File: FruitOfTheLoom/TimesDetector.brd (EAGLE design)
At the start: 73 x 68.9 mm, 22 parts

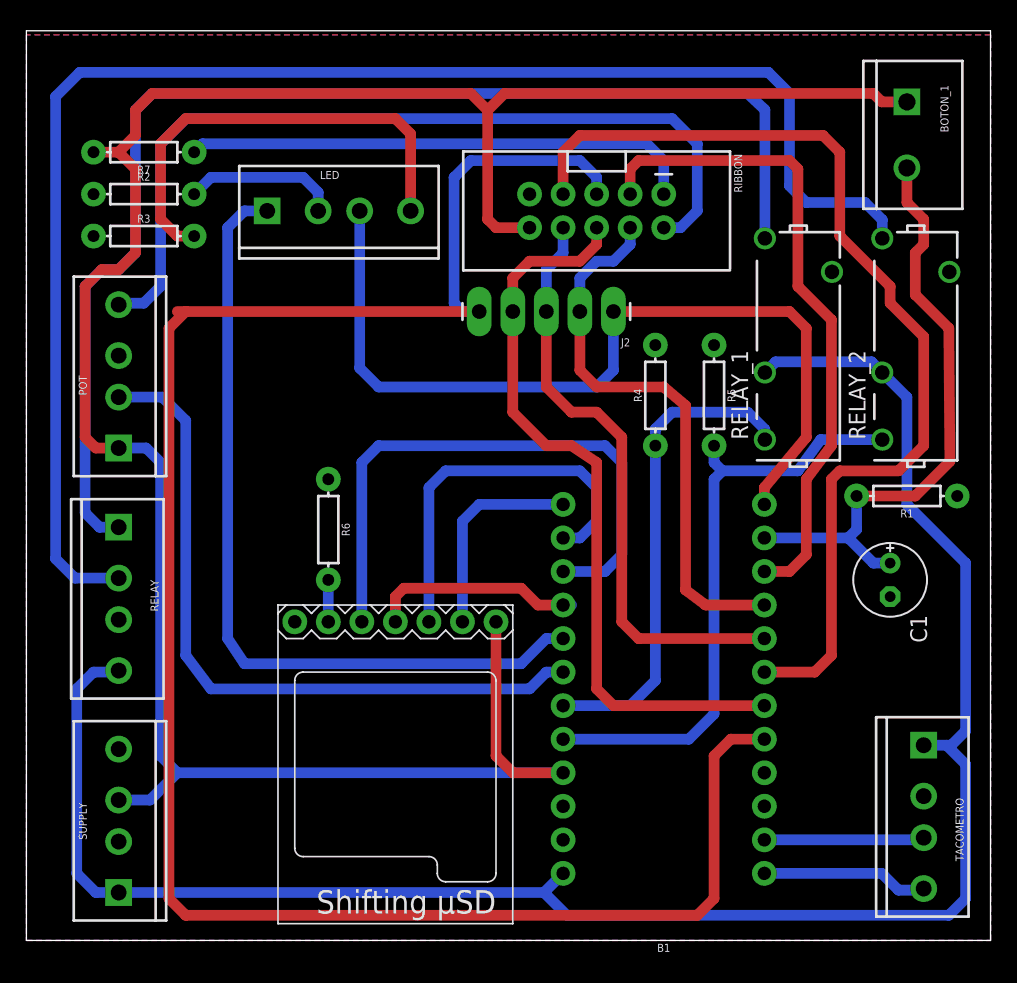
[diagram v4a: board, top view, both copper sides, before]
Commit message: Correcion de pistas, generacion de pdf listos para revelar PCB
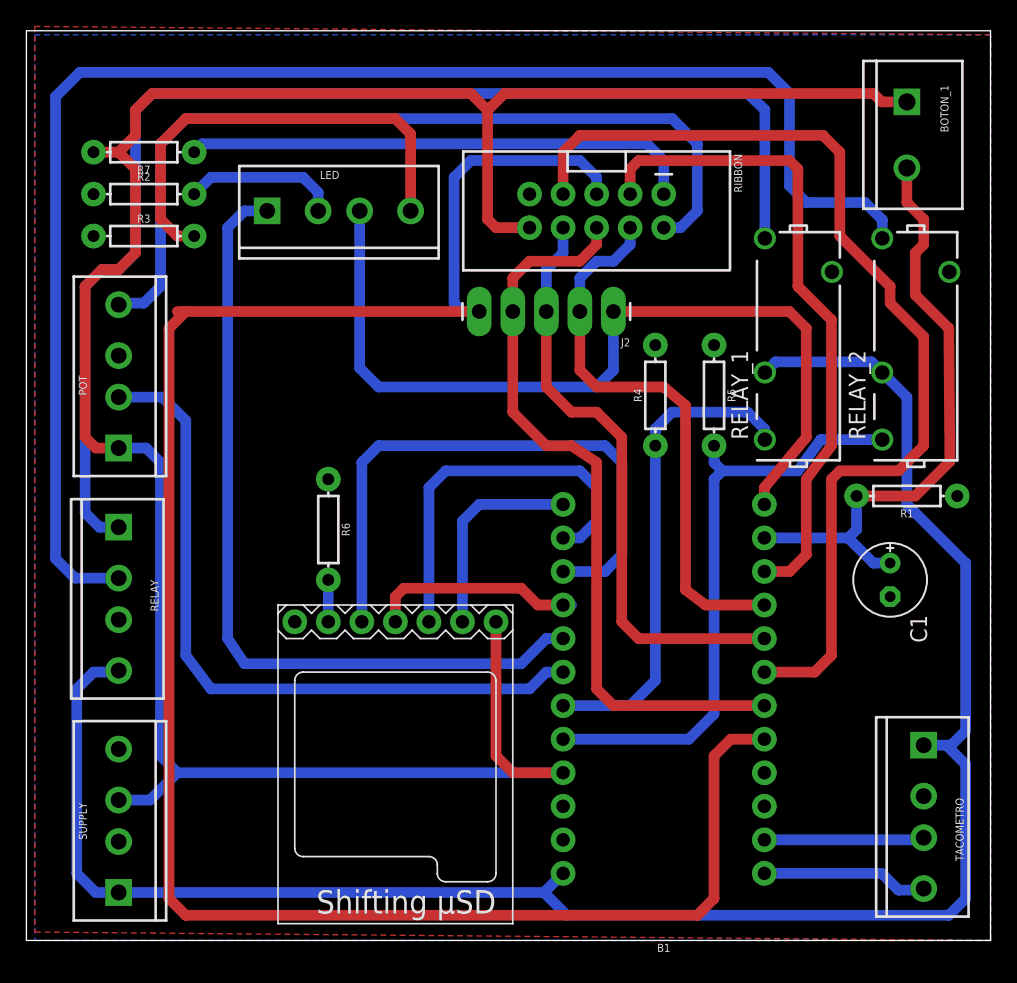
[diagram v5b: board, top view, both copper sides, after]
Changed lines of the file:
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@@
 <grid distance="25" unitdist="mil" unit="inch" style="lines" multiple="1" display="yes" altdistance="5" altunitdist="mil" altunit="inch"/>
 <layers>
-<layer number="1" name="Top" color="4" fill="1" visible="yes" active="yes"/>
+<layer number="1" name="Top" color="4" fill="1" visible="no" active="yes"/>
 <layer number="2" name="Route2" color="1" fill="3" visible="no" active="no"/>
 <layer number="3" name="Route3" color="4" fill="3" visible="no" active="no"/>
@@
 <layer number="19" name="Unrouted" color="6" fill="1" visible="yes" active="yes"/>
 <layer number="20" name="Dimension" color="24" fill="1" visible="yes" active="yes"/>
-<layer number="21" name="tPlace" color="7" fill="1" visible="yes" active="yes"/>
-<layer number="22" name="bPlace" color="7" fill="1" visible="yes" active="yes"/>
-<layer number="23" name="tOrigins" color="15" fill="1" visible="yes" active="yes"/>
-<layer number="24" name="bOrigins" color="15" fill="1" visible="yes" active="yes"/>
-<layer number="25" name="tNames" color="7" fill="1" visible="yes" active="yes"/>
-<layer number="26" name="bNames" color="7" fill="1" visible="yes" active="yes"/>
-<layer number="27" name="tValues" color="7" fill="1" visible="yes" active="yes"/>
-<layer number="28" name="bValues" color="7" fill="1" visible="yes" active="yes"/>
+<layer number="21" name="tPlace" color="7" fill="1" visible="no" active="yes"/>
+<layer number="22" name="bPlace" color="7" fill="1" visible="no" active="yes"/>
+<layer number="23" name="tOrigins" color="15" fill="1" visible="no" active="yes"/>
+<layer number="24" name="bOrigins" color="15" fill="1" visible="no" active="yes"/>
+<layer number="25" name="tNames" color="7" fill="1" visible="no" active="yes"/>
+<layer number="26" name="bNames" color="7" fill="1" visible="no" active="yes"/>
+<layer number="27" name="tValues" color="7" fill="1" visible="no" active="yes"/>
+<layer number="28" name="bValues" color="7" fill="1" visible="no" active="yes"/>
 <layer number="29" name="tStop" color="7" fill="3" visible="no" active="yes"/>
 <layer number="30" name="bStop" color="7" fill="6" visible="no" active="yes"/>
@@
 <layer number="46" name="Milling" color="3" fill="1" visible="no" active="yes"/>
 <layer number="47" name="Measures" color="7" fill="1" visible="no" active="yes"/>
-<layer number="48" name="Document" color="7" fill="1" visible="yes" active="yes"/>
-<layer number="49" name="Reference" color="7" fill="1" visible="yes" active="yes"/>
+<layer number="48" name="Document" color="7" fill="1" visible="no" active="yes"/>
+<layer number="49" name="Reference" color="7" fill="1" visible="no" active="yes"/>
 <layer number="50" name="dxf" color="7" fill="1" visible="no" active="no"/>
-<layer number="51" name="tDocu" color="7" fill="1" visible="yes" active="yes"/>
-<layer number="52" name="bDocu" color="7" fill="1" visible="yes" active="yes"/>
+<layer number="51" name="tDocu" color="7" fill="1" visible="no" active="yes"/>
+<layer number="52" name="bDocu" color="7" fill="1" visible="no" active="yes"/>
 <layer number="53" name="tGND_GNDA" color="7" fill="9" visible="no" active="no"/>
 <layer number="54" name="bGND_GNDA" color="1" fill="9" visible="no" active="no"/>
@@
 <layer number="99" name="SpiceOrder" color="7" fill="1" visible="no" active="no"/>
 <layer number="100" name="Muster" color="7" fill="1" visible="no" active="no"/>
-<layer number="101" name="Patch_Top" color="12" fill="4" visible="yes" active="yes"/>
-<layer number="102" name="Vscore" color="7" fill="1" visible="yes" active="yes"/>
-<layer number="103" name="tMap" color="7" fill="1" visible="yes" active="yes"/>
-<layer number="104" name="Name" color="16" fill="1" visible="yes" active="yes"/>
-<layer number="105" name="tPlate" color="7" fill="1" visible="yes" active="yes"/>
-<layer number="106" name="bPlate" color="7" fill="1" visible="yes" active="yes"/>
+<layer number="101" name="Patch_Top" color="12" fill="4" visible="no" active="yes"/>
+<layer number="102" name="Vscore" color="7" fill="1" visible="no" active="yes"/>
+<layer number="103" name="tMap" color="7" fill="1" visible="no" active="yes"/>
+<layer number="104" name="Name" color="16" fill="1" visible="no" active="yes"/>
+<layer number="105" name="tPlate" color="7" fill="1" visible="no" active="yes"/>
+<layer number="106" name="bPlate" color="7" fill="1" visible="no" active="yes"/>
 <layer number="107" name="Crop" color="7" fill="1" visible="yes" active="yes"/>
 <layer number="108" name="tplace-old" color="10" fill="1" visible="yes" active="yes"/>
@@
 <contactref element="RELAY" pad="3"/>
 <polygon width="0.1524" layer="16" isolate="0.6096">
-<vertex x="-0.635" y="68.58"/>
-<vertex x="-0.635" y="0"/>
+<vertex x="0" y="68.58"/>
+<vertex x="0" y="0"/>
 <vertex x="72.39" y="0"/>
 <vertex x="72.39" y="68.58"/>
@@
 <contactref element="R6" pad="P$1"/>
 <contactref element="R4" pad="P$2"/>
-<polygon width="0.0762" layer="1" isolate="0.6096">
-<vertex x="-0.635" y="68.58"/>
-<vertex x="-0.635" y="0"/>
+<polygon width="0.1524" layer="1" isolate="0.6096">
+<vertex x="0" y="69.215"/>
+<vertex x="0" y="0.635"/>
 <vertex x="72.39" y="0"/>
 <vertex x="72.39" y="68.58"/>
